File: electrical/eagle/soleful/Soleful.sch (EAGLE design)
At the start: 98 parts, among them CN1 To Battery, CN2 Ext Power, IC1 STM32F405RGT, IC3 MCP73833-UN, IC4 LT1129-3.3, Q4 32.768kHz, SW1 RST, SW2 USR, U1 USB Power, Y1 12 MHz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

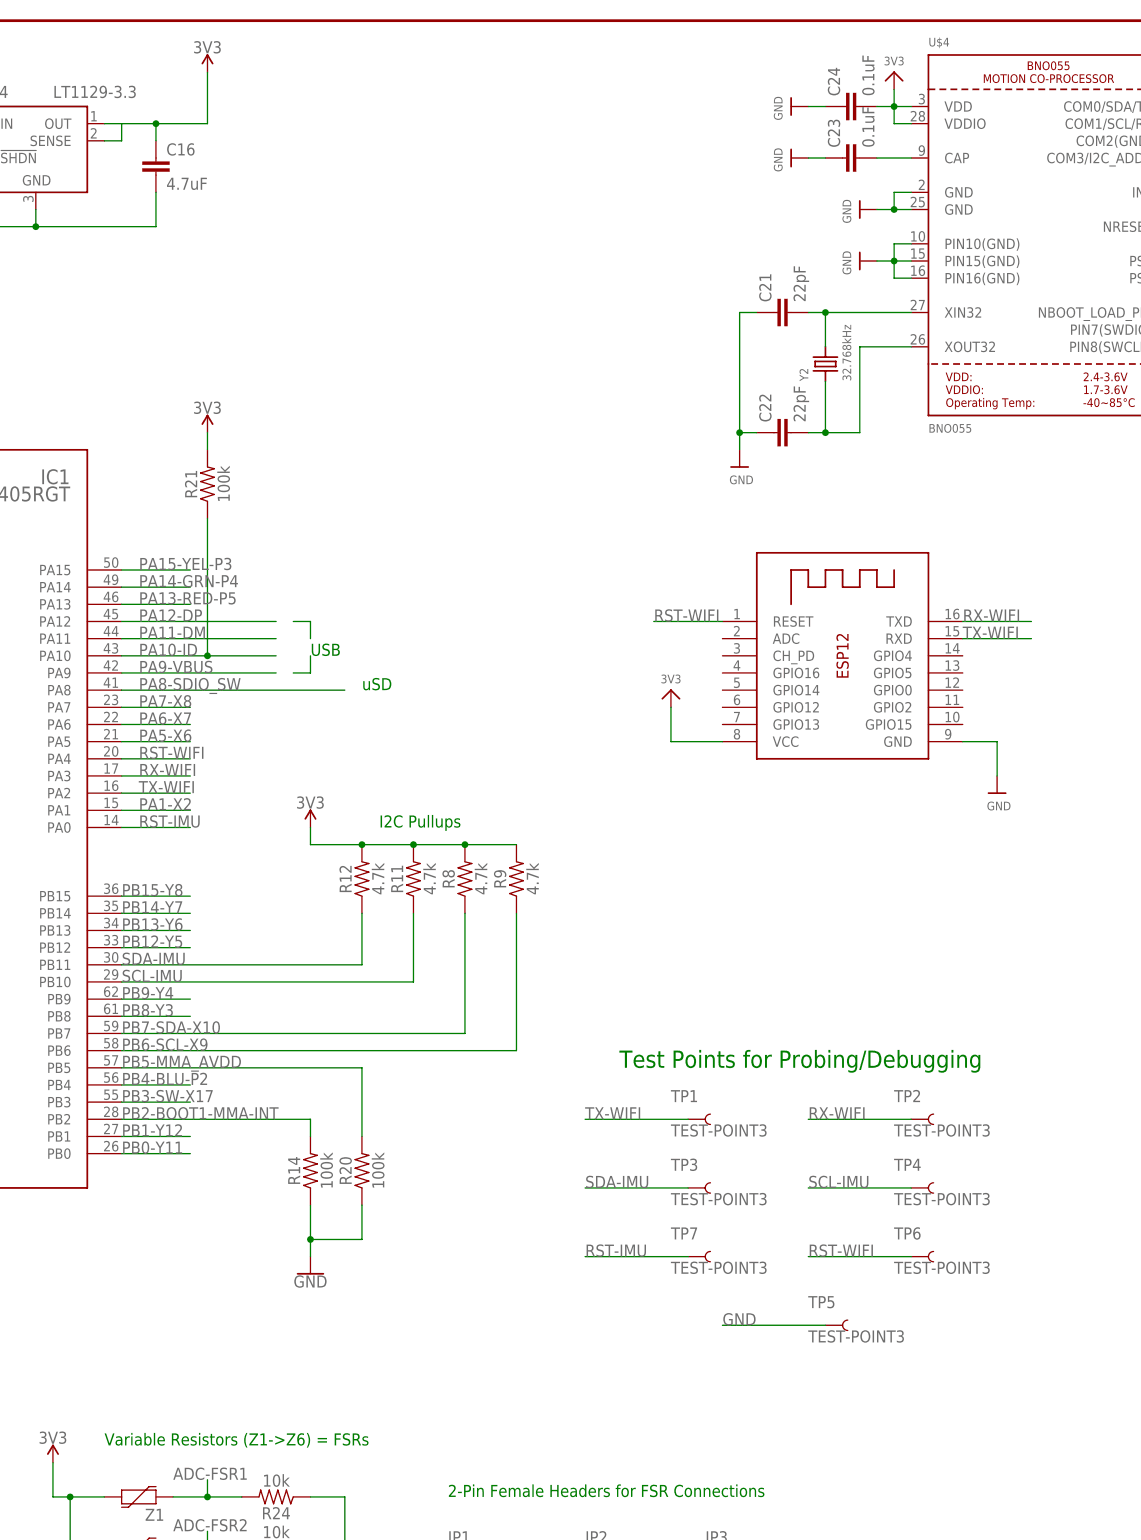
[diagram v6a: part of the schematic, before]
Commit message: Added FETs for power cycling
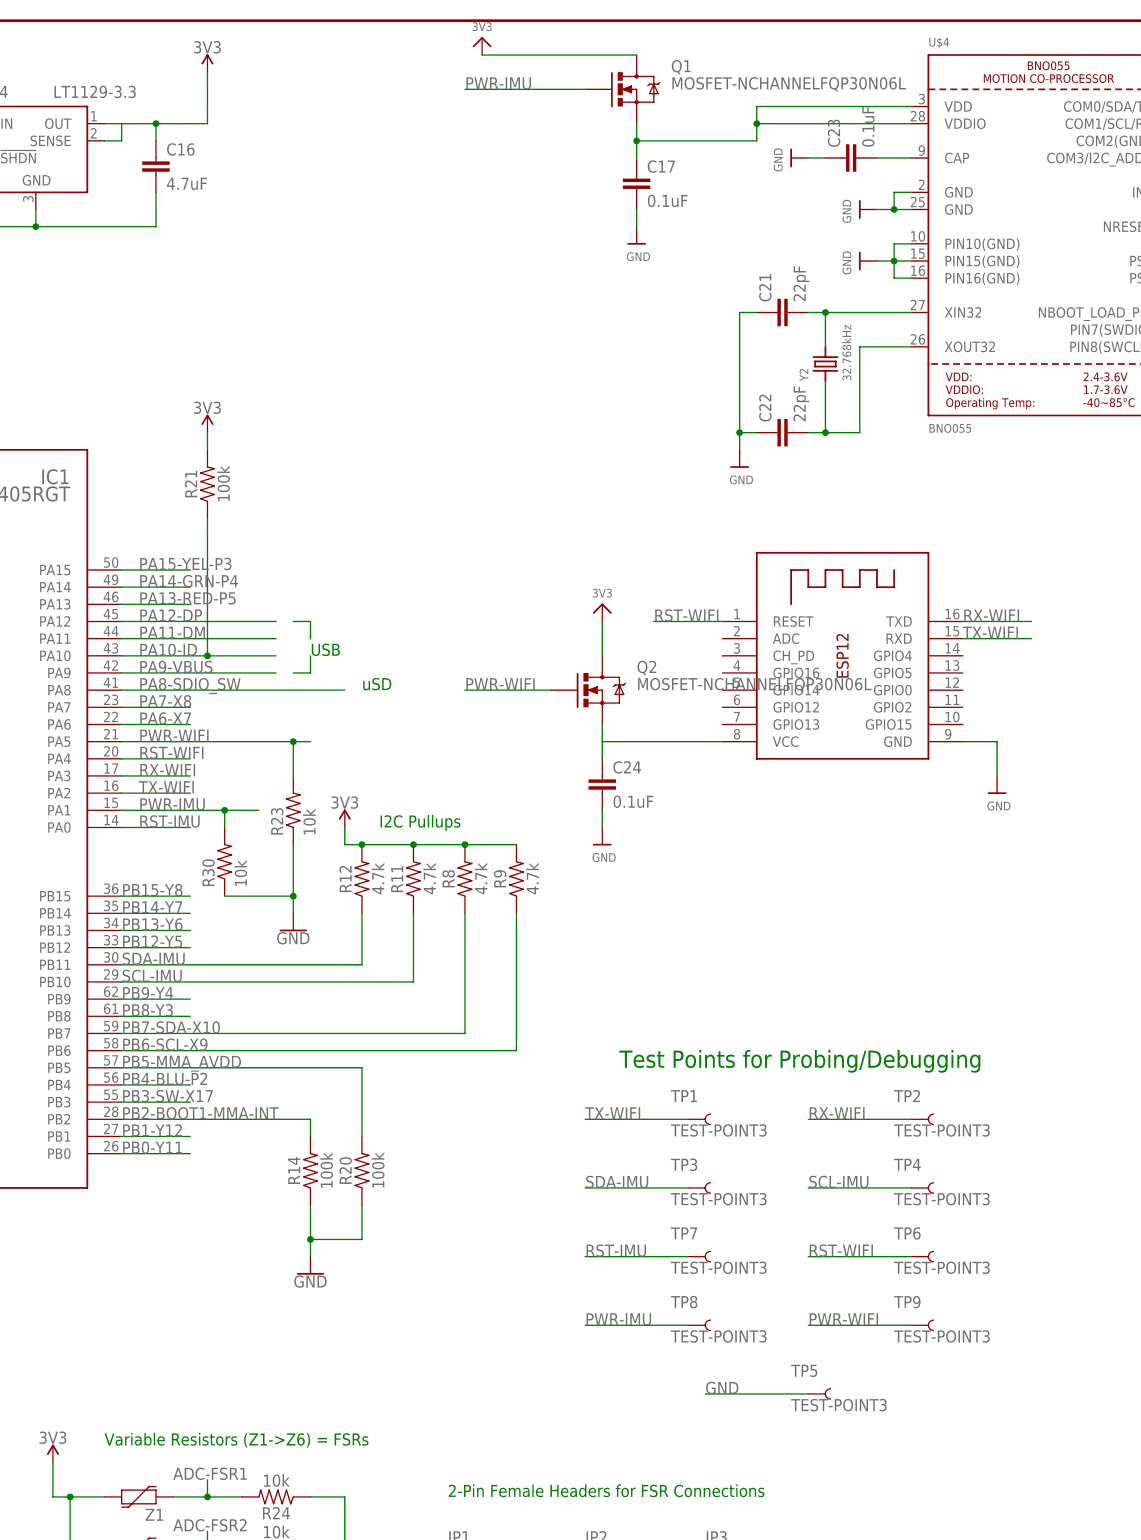
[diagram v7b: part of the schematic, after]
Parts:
- added C17: 0.1uF, SparkFun-Capacitors:CAP0603-CAP
- added Q1, Q2: MOSFET-NCHANNELFQP30N06L, SparkFun-DiscreteSemi:MOSFET-NCHANNELFQP30N06L
- added R23, R30: 10k, SparkFun-Resistors:10KOHM1/10W1%(0603)
- added TP8, TP9: TEST-POINT3, MD-Passives:TEST-POINT3
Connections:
- removed net PA1-X2: IC1.PA1
- removed net PA5-X6: IC1.PA5
- new net N$16: Q2.S, X1.VCC
- new net N$17: C17.1, Q1.S, U$4.VDD, U$4.VDDIO
- new net N$19: C24.1
- new net PWR-IMU: IC1.PA1, Q1.G, R30.2, TP8.1
- new net PWR-WIFI: IC1.PA5, Q2.G, R23.2, TP9.1
- net 3V3: now also Q1.D, Q2.D; no longer C24.2, U$4.VDD, U$4.VDDIO, X1.VCC
- net GND: now also C17.2, C24.2, R23.1, R30.1; no longer C24.1
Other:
- moved on the sheet: C24, TP5
